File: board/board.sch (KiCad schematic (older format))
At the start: 29 parts, among them J1 RPi_Header, J2 Smoke_Sensor, J3 LEDs, J4 Temp_Sensor, J5 Alarm, J6 Conn_01x03, J7 Fan_Power, J8 USB_Power, J9 Coil, Q1 Q_PMOS_GDS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

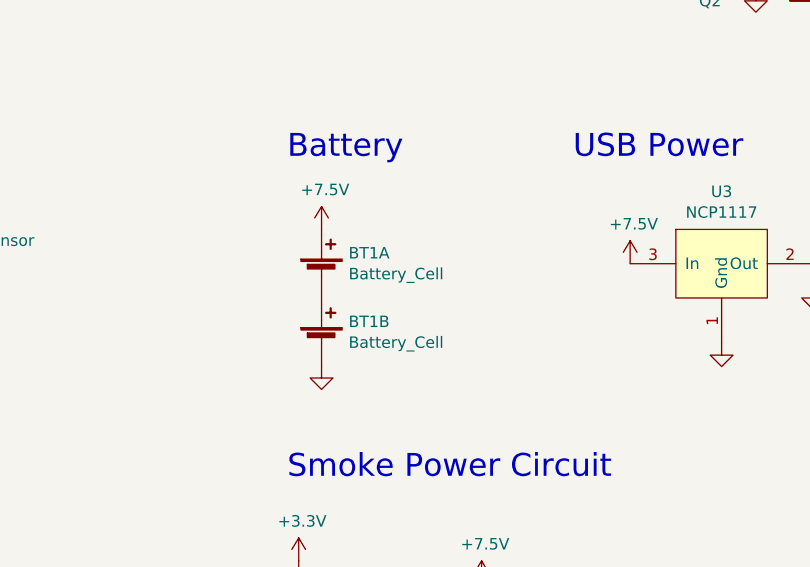
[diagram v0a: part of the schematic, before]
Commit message: Fixed and panelized
Added text to RS232 board
Added on/off switch to main board
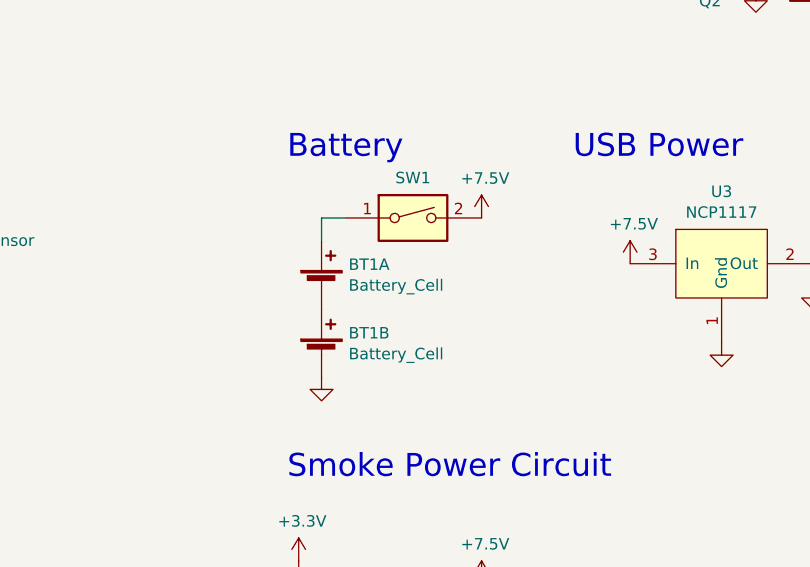
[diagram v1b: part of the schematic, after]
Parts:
- added SW1: SW_DIP_x01, Button_Switch_THT:SW_DIP_SPSTx01_Slide_6.7x4.1mm_W7.62mm_P2.54mm_LowProfile, symbol Switch:SW_DIP_x01
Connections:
- net +7.5V: now also SW1.2; no longer BT1.1 (+)
- new net: BT1.1 (+), SW1.1
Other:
- moved on the sheet: BT1A, BT1B
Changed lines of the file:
@@
 EESchema Schematic File Version 4
+LIBS:board-cache
 EELAYER 26 0
 EELAYER END
@@
 L power:GND #PWR017
 U 1 1 5D5C5B4B
-P 7050 3900
-F 0 "#PWR017" H 7050 3650 50  0001 C CNN
-F 1 "GND" H 7055 3727 50  0001 C CNN
-F 2 "" H 7050 3900 50  0001 C CNN
-F 3 "" H 7050 3900 50  0001 C CNN
-	1    7050 3900
+P 7050 3950
+F 0 "#PWR017" H 7050 3700 50  0001 C CNN
+F 1 "GND" H 7055 3777 50  0001 C CNN
+F 2 "" H 7050 3950 50  0001 C CNN
+F 3 "" H 7050 3950 50  0001 C CNN
+	1    7050 3950
 	1    0    0    -1
 $EndComp
@@
 L power:+7.5V #PWR016
 U 1 1 5D5C5B7F
-P 7050 3300
-F 0 "#PWR016" H 7050 3150 50  0001 C CNN
-F 1 "+7.5V" H 7065 3473 50  0000 C CNN
-F 2 "" H 7050 3300 50  0001 C CNN
-F 3 "" H 7050 3300 50  0001 C CNN
-	1    7050 3300
+P 7750 3250
+F 0 "#PWR016" H 7750 3100 50  0001 C CNN
+F 1 "+7.5V" H 7765 3423 50  0000 C CNN
+F 2 "" H 7750 3250 50  0001 C CNN
+F 3 "" H 7750 3250 50  0001 C CNN
+	1    7750 3250
 	1    0    0    -1
 $EndComp
@@
 L custom:Battery_Cell BT1
 U 1 1 5D629C2C
-P 7050 3500
-F 0 "BT1" H 7168 3596 50  0000 L CNN
-F 1 "Battery_Cell" H 7168 3505 50  0000 L CNN
-F 2 "custom:Keystone_1048_2x18650" V 7050 3560 50  0001 C CNN
-F 3 "~" V 7050 3560 50  0001 C CNN
-	1    7050 3500
+P 7050 3550
+F 0 "BT1" H 7168 3646 50  0000 L CNN
+F 1 "Battery_Cell" H 7168 3555 50  0000 L CNN
+F 2 "custom:Keystone_1048_2x18650" V 7050 3610 50  0001 C CNN
+F 3 "~" V 7050 3610 50  0001 C CNN
+	1    7050 3550
 	1    0    0    -1
 $EndComp
@@
 L custom:Battery_Cell BT1
 U 2 1 5D629CEA
-P 7050 3800
-F 0 "BT1" H 7168 3896 50  0000 L CNN
-F 1 "Battery_Cell" H 7168 3805 50  0000 L CNN
-F 2 "custom:Keystone_1048_2x18650" V 7050 3860 50  0001 C CNN
-F 3 "~" V 7050 3860 50  0001 C CNN
-	2    7050 3800
+P 7050 3850
+F 0 "BT1" H 7168 3946 50  0000 L CNN
+F 1 "Battery_Cell" H 7168 3855 50  0000 L CNN
+F 2 "custom:Keystone_1048_2x18650" V 7050 3910 50  0001 C CNN
+F 3 "~" V 7050 3910 50  0001 C CNN
+	2    7050 3850
 	1    0    0    -1
 $EndComp
@@
 	10450 6150 10450 6200
 Connection ~ 10450 6150
+$Comp
+L Switch:SW_DIP_x01 SW1
+U 1 1 5D5DB8A3
+P 7450 3250
+F 0 "SW1" H 7450 3425 50  0000 C CNN
+F 1 "SW_DIP_x01" H 7450 3426 50  0001 C CNN
+F 2 "Button_Switch_THT:SW_DIP_SPSTx01_Slide_6.7x4.1mm_W7.62mm_P2.54mm_LowProfile" H 7450 3250 50  0001 C CNN
+F 3 "" H 7450 3250 50  0001 C CNN
+	1    7450 3250
+	1    0    0    -1
+$EndComp
+Wire Wire Line
+	7050 3350 7050 3250
+Wire Wire Line
+	7050 3250 7150 3250
 $EndSCHEMATC
